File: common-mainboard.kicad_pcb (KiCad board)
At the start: 2 copper layers, 77.5 x 50.8 mm, 100 parts, among them J1 SIM_Card, J2 RSP-122811-01, J3 Conn_01x02_Female, J4 S4B-ZR-SM4A-TF(LF)(SN), J5 S4B-ZR-SM4A-TF(LF)(SN), J6 S6B-ZR-SM4A-TF(LF)(SN), Q1 DTC043ZEB, Q2 DTC043ZEB, Q3 DTC043ZEB, SW1 SW_Push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

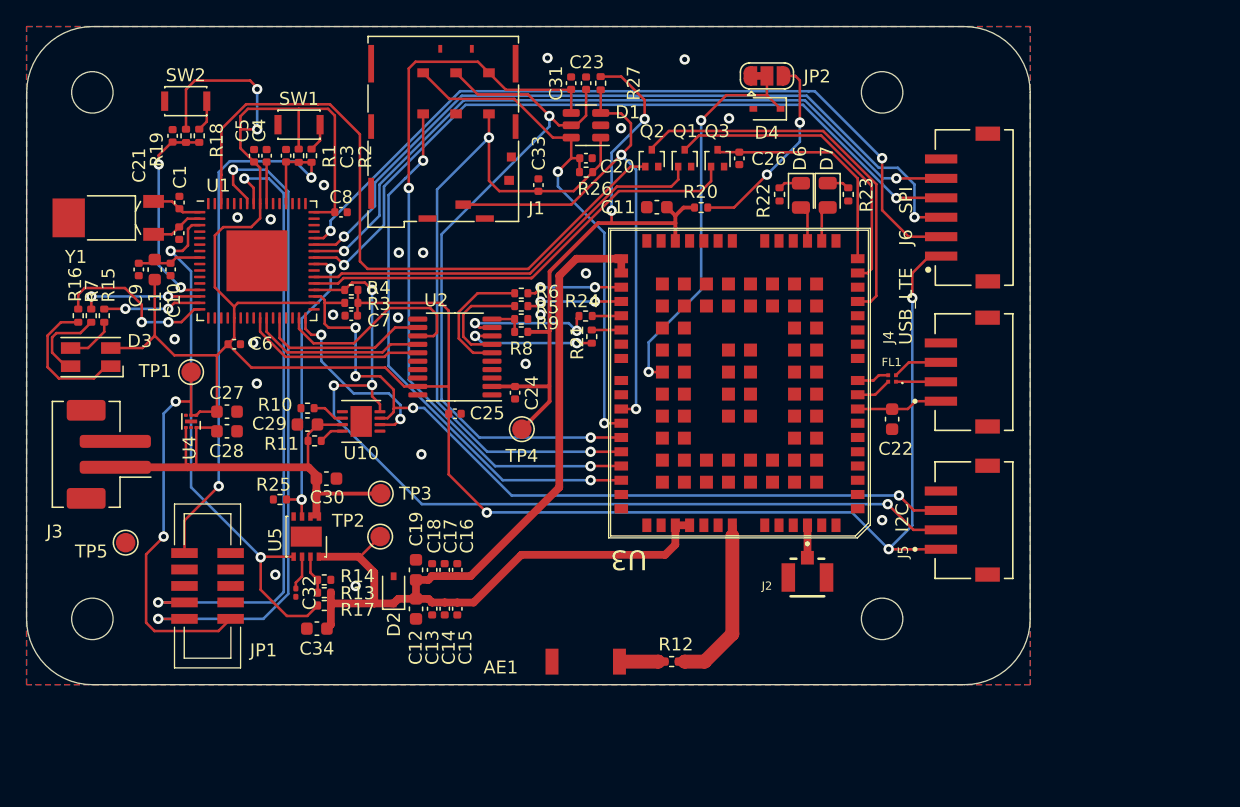
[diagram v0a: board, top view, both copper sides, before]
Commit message: [FAB] added board dimensions
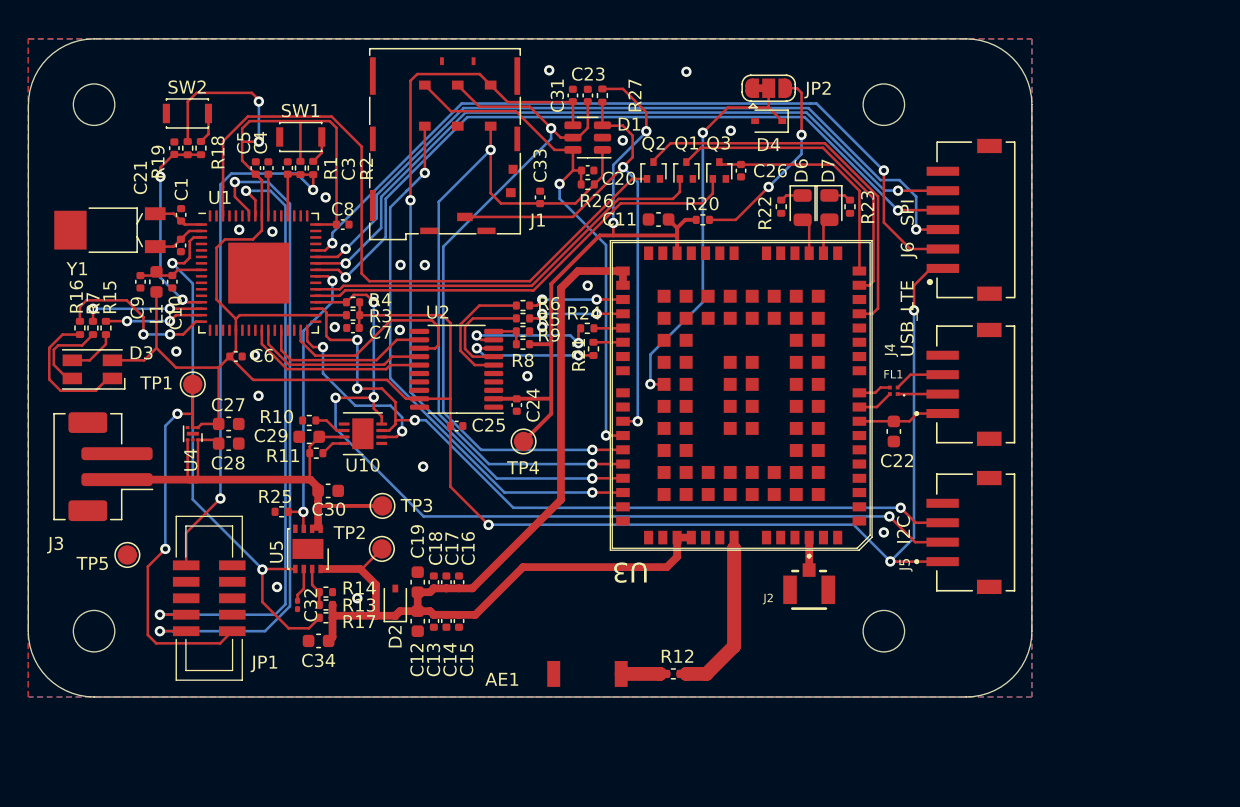
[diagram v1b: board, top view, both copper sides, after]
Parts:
- moved AE1 0.96 mm to (152.0, 130.2)
- moved C22 0.96 mm to (176.0, 106.5)
- moved J4 0.96 mm to (179.8, 102.9)
- moved J5 0.96 mm to (179.8, 114.3)
- moved Q1 0.96 mm to (160.0, 86.4)
- moved R17 0.96 mm to (132.2, 120.9)
- moved R3 0.96 mm to (134.3, 97.5)
- moved R4 0.96 mm to (134.3, 96.5)
- moved SW1 0.96 mm to (130.3, 83.8)
- moved U10 0.96 mm to (135.1, 106.7)
- moved C1 0.96 mm to (121.0, 89.8)
- moved C2 0.96 mm to (121.0, 92.1)
- moved C21 0.96 mm to (120.5, 84.6)
- moved C5 0.96 mm to (126.8, 86.2)
- moved C6 0.96 mm to (125.3, 100.7)
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
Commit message: PCB: moved vias from underneath to outside of ICs
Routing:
- net +3V3: track 217.8 -> 226.5 mm, vias 7 -> 8
- net USB_BOOT: track 31.0 -> 36.0 mm
- net USIM1_VDD: track 40.5 -> 43.4 mm
- net USIM1_DET: track 42.2 -> 43.9 mm
- net GNDREF: vias 21 -> 19

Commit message: ok before switching to EG91EX footprint
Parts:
- C12, C16: footprint Capacitor_SMD:C_0603_1608Metric -> Capacitor_Tantalum_SMD:CP_EIA-6032-15_Kemet-U
- C32: footprint Capacitor_SMD:C_0201_0603Metric -> Capacitor_SMD:C_0402_1005Metric
- D2, D4: footprint Diode_SMD:D_SOD-323 -> Diode_SMD:D_SOD-323_HandSoldering
- R10, R13: footprint Resistor_SMD:R_0402_1005Metric -> Resistor_SMD:R_0603_1608Metric
- SW1, SW2: footprint Button_Switch_SMD:SW_SPST_CK_KXT3 -> Button_Switch_SMD:SW_Push_1P1T_NO_CK_KMR2
- moved C16 3.91 mm to (140.7, 114.5)
- moved C19 3.39 mm to (145.4, 116.5)
- moved C18 3.37 mm to (144.4, 116.5)
- moved C17 3.37 mm to (143.5, 116.5)
- moved C14 3.09 mm to (144.5, 120.3)
- moved C13 3.09 mm to (143.5, 120.3)
- moved C15 3.09 mm to (145.4, 120.3)
- moved C12 1.79 mm to (140.7, 122.2)
- moved C34 0.79 mm to (132.2, 122.1)
- moved SW2 0.68 mm to (121.5, 81.3)
- moved SW1 0.66 mm to (129.8, 83.3)
- moved R14 0.52 mm to (132.2, 118.4)
- moved R17 0.32 mm to (132.5, 120.9)
- moved R13 0.26 mm to (132.2, 119.6)
- moved R10 0.25 mm to (130.9, 105.4)
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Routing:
- net +3V3: track 226.5 -> 230.8 mm
- net UC_PWRKEY_DCE: track 53.6 -> 55.4 mm
- net GNDREF: vias 19 -> 20

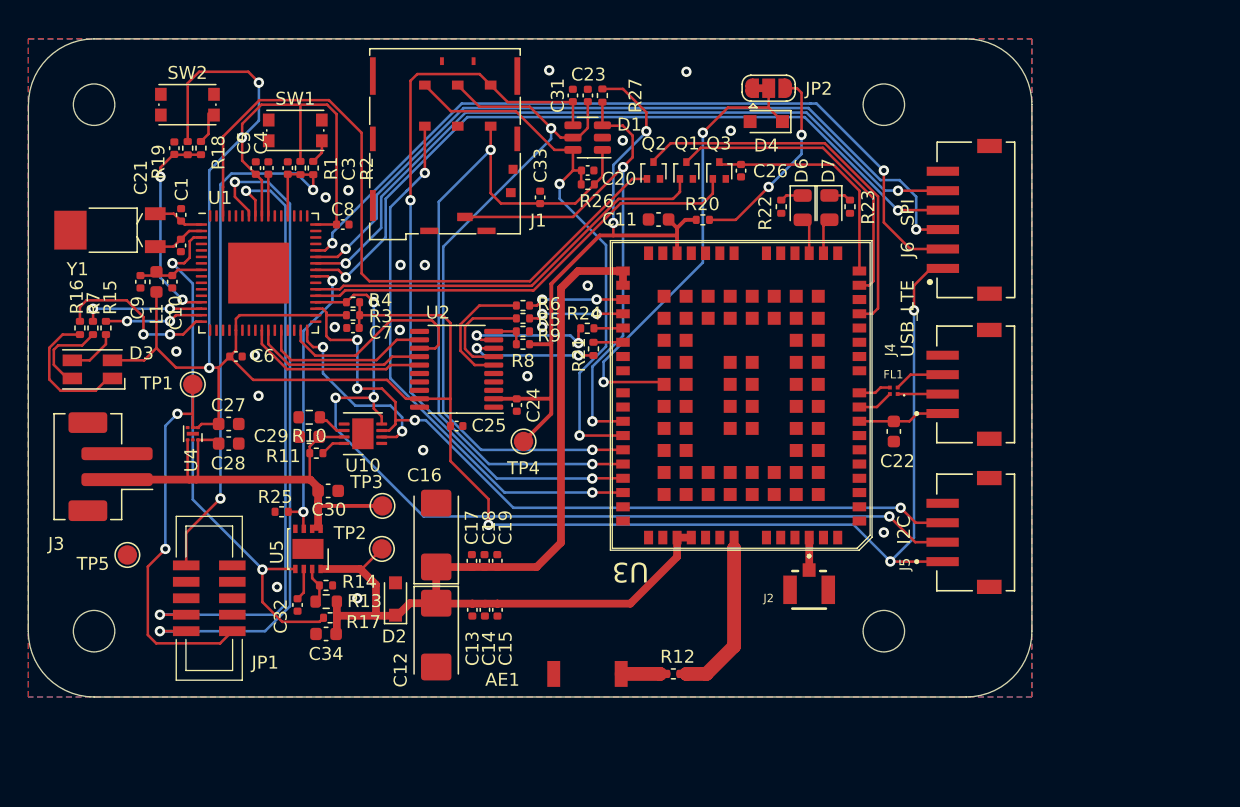
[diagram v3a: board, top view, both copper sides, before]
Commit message: Added IO and debug UART to pin header
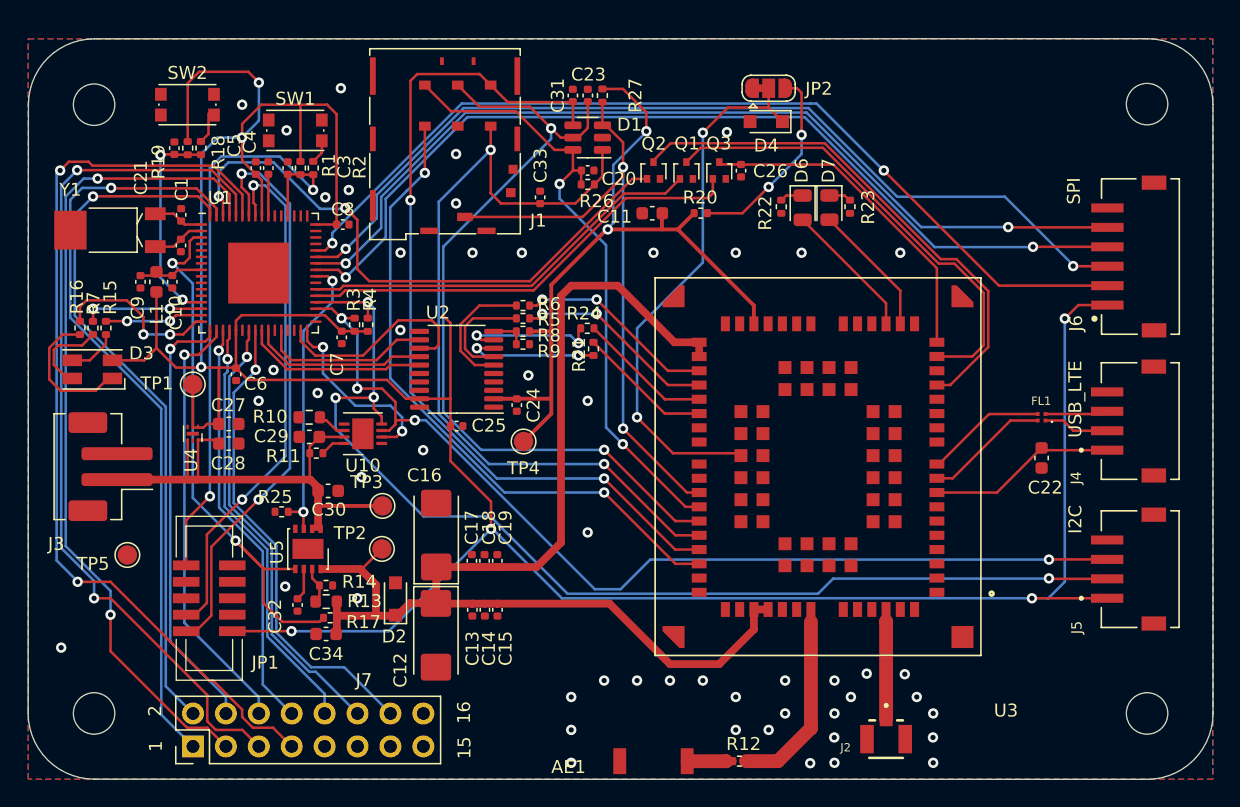
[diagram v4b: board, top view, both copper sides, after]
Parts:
- added J7: Conn_02x10_Odd_Even, Connector_PinHeader_2.54mm:PinHeader_2x08_P2.54mm_Vertical, F.Cu at (121.9, 130.8)
- U3: footprint quectel-lib:_AD LIB_EG915U.PcbLib_EG915U -> EG91EXGA-128-SGNS:XCVR_EG91EXGA-128-SGNS
- moved H2 21.3 mm to (195.6, 128.3)
- moved H3 20.3 mm to (195.6, 81.2)
- moved J6 13.0 mm to (192.5, 93.0)
- moved J4 13.0 mm to (192.5, 105.7)
- moved J5 13.0 mm to (192.5, 117.1)
- moved J2 13.0 mm to (175.4, 130.3)
- moved FL1 11.6 mm to (187.4, 105.4)
- moved C22 11.6 mm to (187.4, 108.5)
- moved G*** 10.2 mm to (156.2, 105.4)
- moved R12 8.44 mm to (164.1, 132.0)
- moved AE1 8.44 mm to (157.1, 137.0)
- moved U3 8.09 mm to (170.2, 109.2)
- moved H1 6.35 mm to (114.3, 128.3)
- moved R4 2.07 mm to (135.4, 98.3), turned to 90 degrees
- moved C6 1.37 mm to (125.3, 102.1), turned to -90 degrees
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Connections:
- U1 pad 17: unconnected-(U1-Pad17) -> DEBUG_TX
- U1 pad 18: unconnected-(U1-Pad18) -> DEBUG_RX
- U1 pad 19: unconnected-(U1-Pad19) -> PA10
- U1 pad 20: unconnected-(U1-Pad20) -> PA11
- U1 pad 23: unconnected-(U1-Pad23) -> PB10
- U1 pad 24: unconnected-(U1-Pad24) -> PB11
- U1 pad 59: unconnected-(U1-Pad59) -> PB30
- U1 pad 60: unconnected-(U1-Pad60) -> PB31
- U1 pad 61: unconnected-(U1-Pad61) -> PB00
- U1 pad 63: unconnected-(U1-Pad63) -> PB02
- U1 pad 64: unconnected-(U1-Pad64) -> PB03
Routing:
- net PB30: track 0.00 -> 71.8 mm, vias 0 -> 2
- net PB31: track 0.00 -> 67.9 mm, vias 0 -> 2
- net PB00: track 0.00 -> 63.9 mm, vias 0 -> 2
- net PB02: track 0.00 -> 59.0 mm, vias 0 -> 1
- net PB03: track 0.00 -> 54.3 mm, vias 0 -> 1
- net PB11: track 0.00 -> 36.8 mm, vias 0 -> 1
- net PB10: track 0.00 -> 34.8 mm, vias 0 -> 1
- net DEBUG_TX: track 0.00 -> 33.9 mm, vias 0 -> 1
- net DEBUG_RX: track 0.00 -> 33.7 mm, vias 0 -> 1
- net PA11: track 0.00 -> 32.9 mm, vias 0 -> 1
- net PA10: track 0.00 -> 32.0 mm, vias 0 -> 1
- net SCL: track 70.4 -> 85.8 mm
- net SDA: track 62.5 -> 76.9 mm
- net VBAT_BB: track 81.9 -> 96.3 mm
- net /CS: track 57.1 -> 71.0 mm
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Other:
- board size 77.5 x 50.8 mm -> 91.5 x 57.2 mm
- board text added: "1"
- board text added: "15"
- board text added: "16"
- board text added: "2"

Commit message: Added 4G modem UART test points
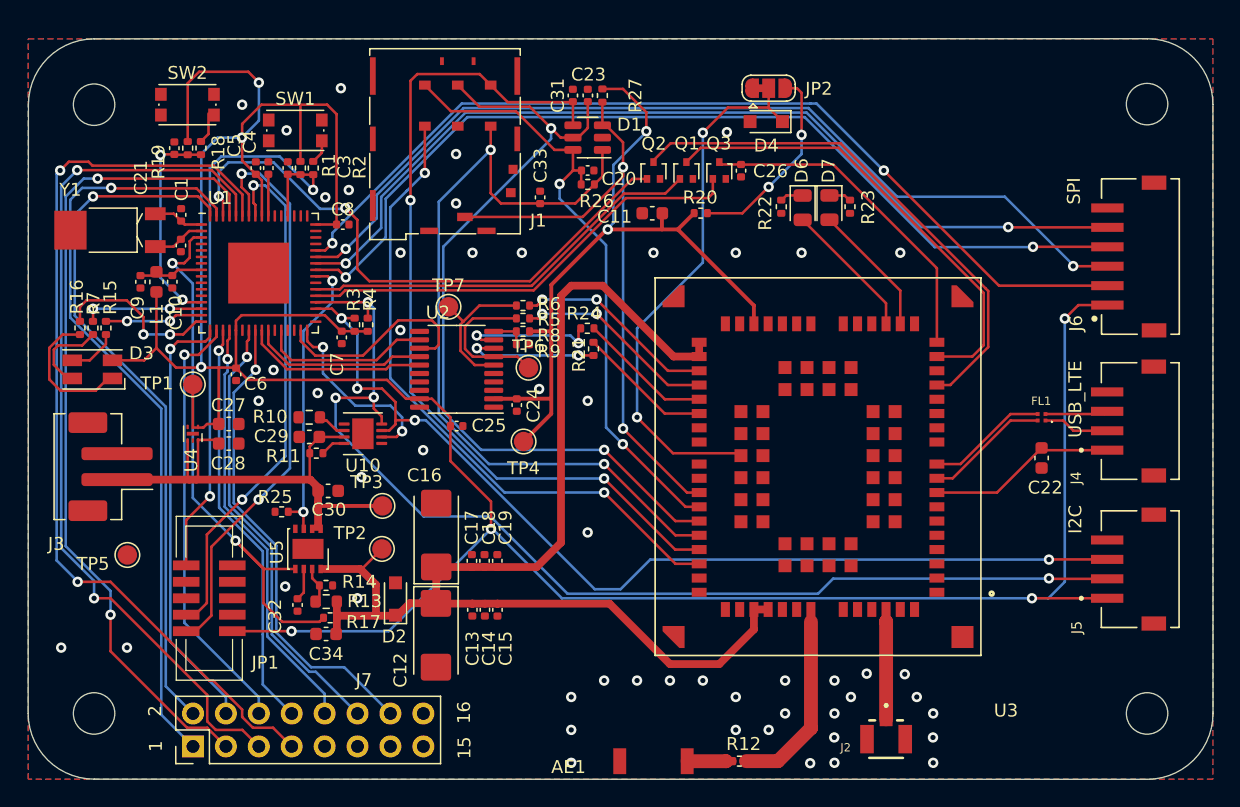
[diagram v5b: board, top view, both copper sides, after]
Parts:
- added TP6: DCE_TX, TestPoint:TestPoint_Pad_D1.5mm, F.Cu at (147.8, 101.6)
- added TP7: DCE_RX, TestPoint:TestPoint_Pad_D1.5mm, F.Cu at (141.7, 96.9)
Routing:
- net +3V3: track 241.4 -> 233.9 mm
- net DCE_TX: track 8.43 -> 11.5 mm
- net DCE_RX: track 9.97 -> 11.6 mm
- net GNDREF: vias 51 -> 52
